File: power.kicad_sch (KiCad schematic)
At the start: 47 parts, among them CN3 DF40C-20DP-0.4V, J2 TYPE-C16PIN, Q5 CSD17575Q3A, Q6 CSD17575Q3A, Q7 CSD17575Q3A, Q8 CSD17575Q3A, U2 CH224K, U3 BQ25792RQMR, U4 AP2112K-3.3TRG1, U5 AP2112K-1.8TRG1, U6 LP8556SQ-E09/NOPB, U8 ESD7104MUTAG_C2987068, U9 TPS61088RHLR

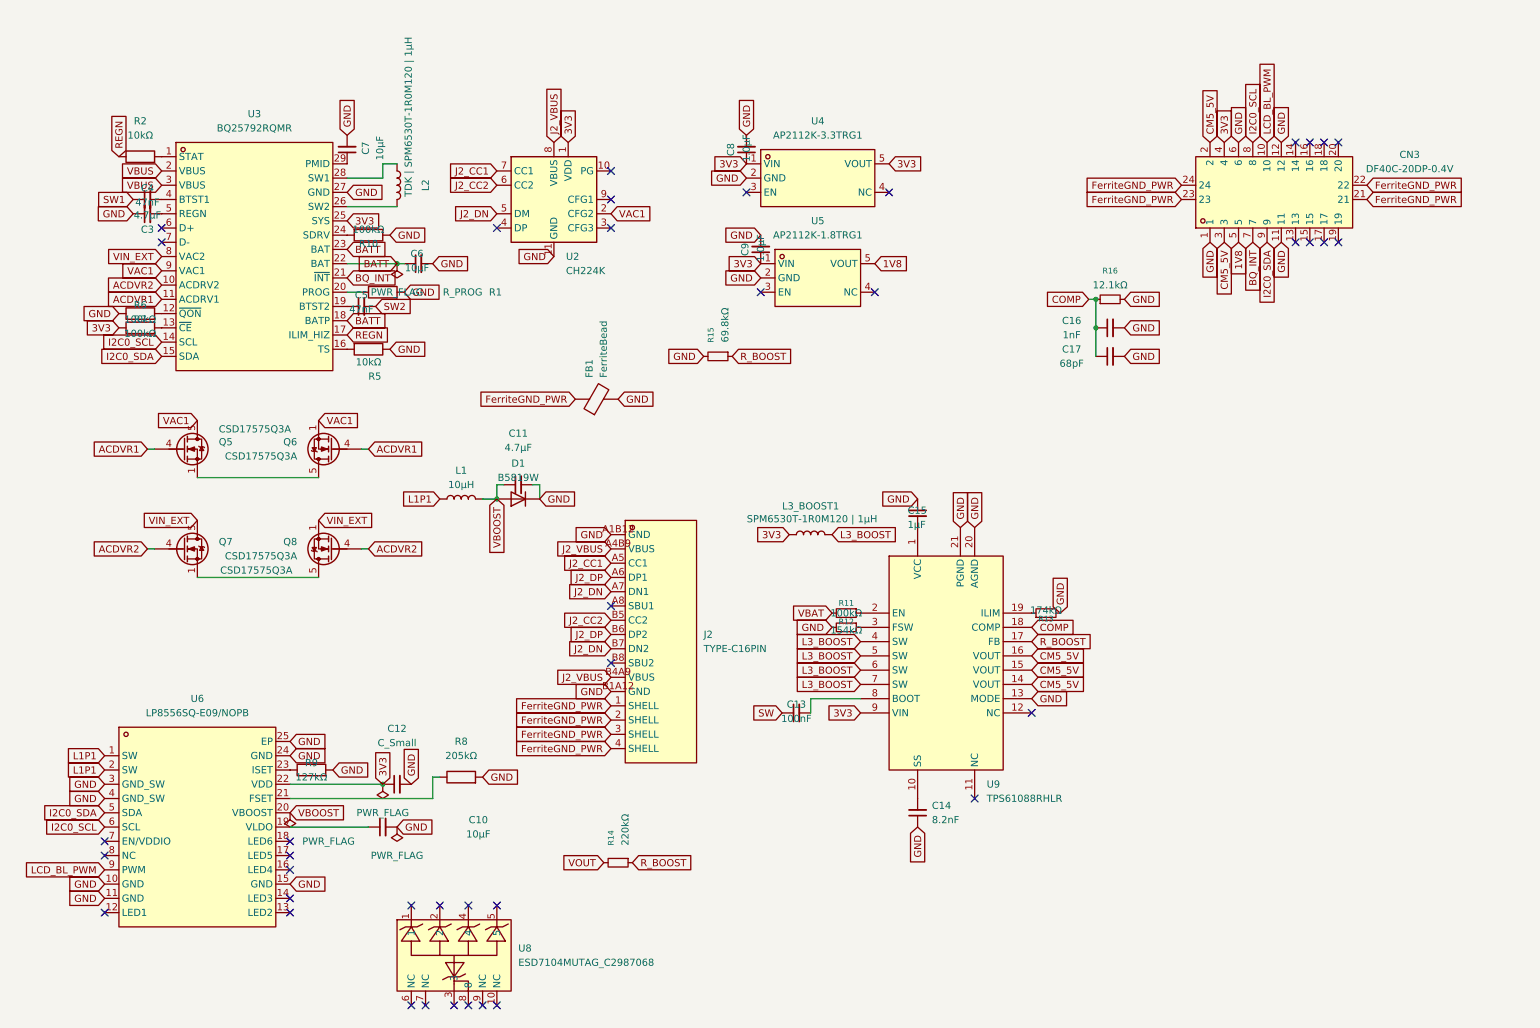
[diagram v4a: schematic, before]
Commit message: finished slateconnect i2c gpio expander, completed led status bar schematic, fixed all drc errors, started assigning footprints and started bom
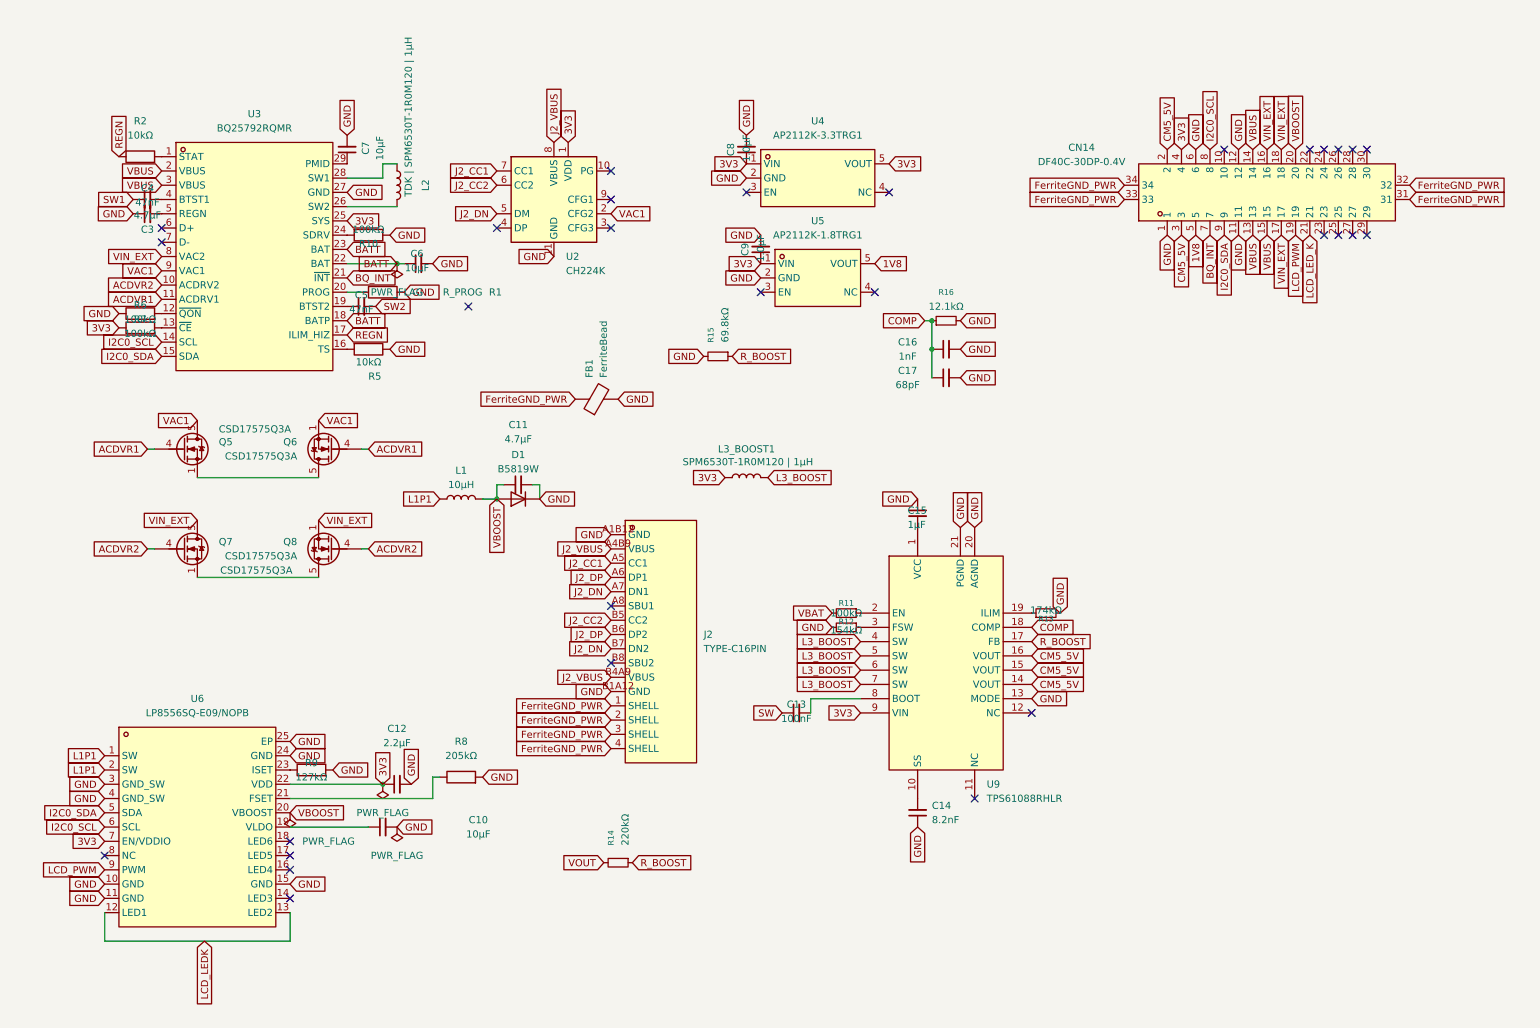
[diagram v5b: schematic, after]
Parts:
- removed CN3: DF40C-20DP-0.4V, slate113:CONN-SMD_20P-P0.40_HRS_DF40TC-20DP-0.4V, symbol slate113:DF40C-20DP-0.4V
- removed U8: ESD7104MUTAG_C2987068, slate113:DFN-10_L2.5-W1.0-P0.50-BL, symbol slate113:ESD7104MUTAG_C2987068
- added CN14: DF40C-30DP-0.4V, slate113:CONN-SMD_30P-P0.40_5001-BM0430-15-00, symbol slate113:DF40C-30DP-0.4V
- C10, C6, C7: footprint (none) -> Capacitor_SMD:C_0603_1608Metric; MPN (none) -> CL10A106KP8NNNC; Manufacturer (none) -> Samsung Electro-Mechanics
- C11, C3: footprint (none) -> Capacitor_SMD:C_0603_1608Metric; MPN (none) -> CL10B475KA8NNNC; Manufacturer (none) -> Samsung Electro-Mechanics
- C12: value C_Small -> 2.2µF; footprint (none) -> Capacitor_SMD:C_0603_1608Metric; MPN (none) -> CL10B225KA8NNNC; Manufacturer (none) -> Samsung Electro-Mechanics
- C13: footprint (none) -> Capacitor_SMD:C_0603_1608Metric; MPN (none) -> CL10B104KB8NNNC; Manufacturer (none) -> Samsung Electro-Mechanics
- C15, C8, C9: footprint (none) -> Capacitor_SMD:C_0603_1608Metric; MPN (none) -> CL10B105KA8NNNC; Manufacturer (none) -> Samsung Electro-Mechanics
- C16: footprint (none) -> Capacitor_SMD:C_0603_1608Metric; MPN (none) -> CL10B102KB8NNNC; Manufacturer (none) -> Samsung Electro-Mechanics
- C17: footprint (none) -> Capacitor_SMD:C_0603_1608Metric; MPN (none) -> CL10C680JB8NNNC; Manufacturer (none) -> Samsung Electro-Mechanics
- C4, C5: footprint (none) -> Capacitor_SMD:C_0603_1608Metric; MPN (none) -> CL10B473KB8NNNC; Manufacturer (none) -> Samsung Electro-Mechanics
- D1: MPN (none) -> B5819W; Manufacturer (none) -> LCSC
- L1: MPN (none) -> TDK SPM6530T-100M; Manufacturer (none) -> DigiKey
- Q5, Q6, Q7, Q8: MPN (none) -> CSD17575Q3A; Manufacturer (none) -> LCSC
- R10, R11, R6, R7: footprint (none) -> Resistor_SMD:R_0603_1608Metric; MPN (none) -> RC0603FR-07100KL; Manufacturer (none) -> Yageo
- R12: footprint (none) -> Resistor_SMD:R_0603_1608Metric; MPN (none) -> RC0603FR-07154KL; Manufacturer (none) -> Yageo
- R13: footprint (none) -> Resistor_SMD:R_0603_1608Metric; MPN (none) -> RC0603FR-07174KL; Manufacturer (none) -> Yageo
- R14: footprint (none) -> Resistor_SMD:R_0603_1608Metric; MPN (none) -> RC0603FR-07220KL; Manufacturer (none) -> Yageo
- R15: footprint (none) -> Resistor_SMD:R_0603_1608Metric; MPN (none) -> RC0603FR-0769K8L; Manufacturer (none) -> Yageo
- R16: footprint (none) -> Resistor_SMD:R_0603_1608Metric; MPN (none) -> RC0603FR-0712K1L; Manufacturer (none) -> Yageo
- R2, R5: footprint (none) -> Resistor_SMD:R_0603_1608Metric; MPN (none) -> RC0603FR-0710KL; Manufacturer (none) -> Yageo
- R8: footprint (none) -> Resistor_SMD:R_0603_1608Metric; MPN (none) -> RC0603FR-07205KL; Manufacturer (none) -> Yageo
- R9: footprint (none) -> Resistor_SMD:R_0603_1608Metric; MPN (none) -> RC0603FR-07127KL; Manufacturer (none) -> Yageo
- U2: MPN (none) -> CH224K; Manufacturer (none) -> LCSC
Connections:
- net 1V8: now also CN14.5
- net 3V3: now also U6.7 (EN/VDDIO), CN14.4
- net BQ_INT: now also CN14.7
- net CM5_5V: now also CN14.2, CN14.3
- net FerriteGND_PWR: now also CN14.31, CN14.32, CN14.33, CN14.34
- net GND: now also CN14.1, CN14.11, CN14.12, CN14.6
- net I2C0_SCL: now also CN14.8
- net I2C0_SDA: now also CN14.9
- net VBOOST: now also CN14.20
- net VBUS: now also CN14.13, CN14.14, CN14.15
- net VIN_EXT: now also CN14.16, CN14.17, CN14.18
- net LCD_LEDK: now reaches U6.12 (LED1)
- net LCD_LEDK: now also U6.13 (LED2)
- net LCD_BL_PWM renamed LCD_PWM
- net LCD_PWM: now also CN14.19
- new net LCD_LED_K: CN14.21
- no-connect marks 40 -> 30
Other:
- moved on the sheet: C16, C17, L3_BOOST1, R16

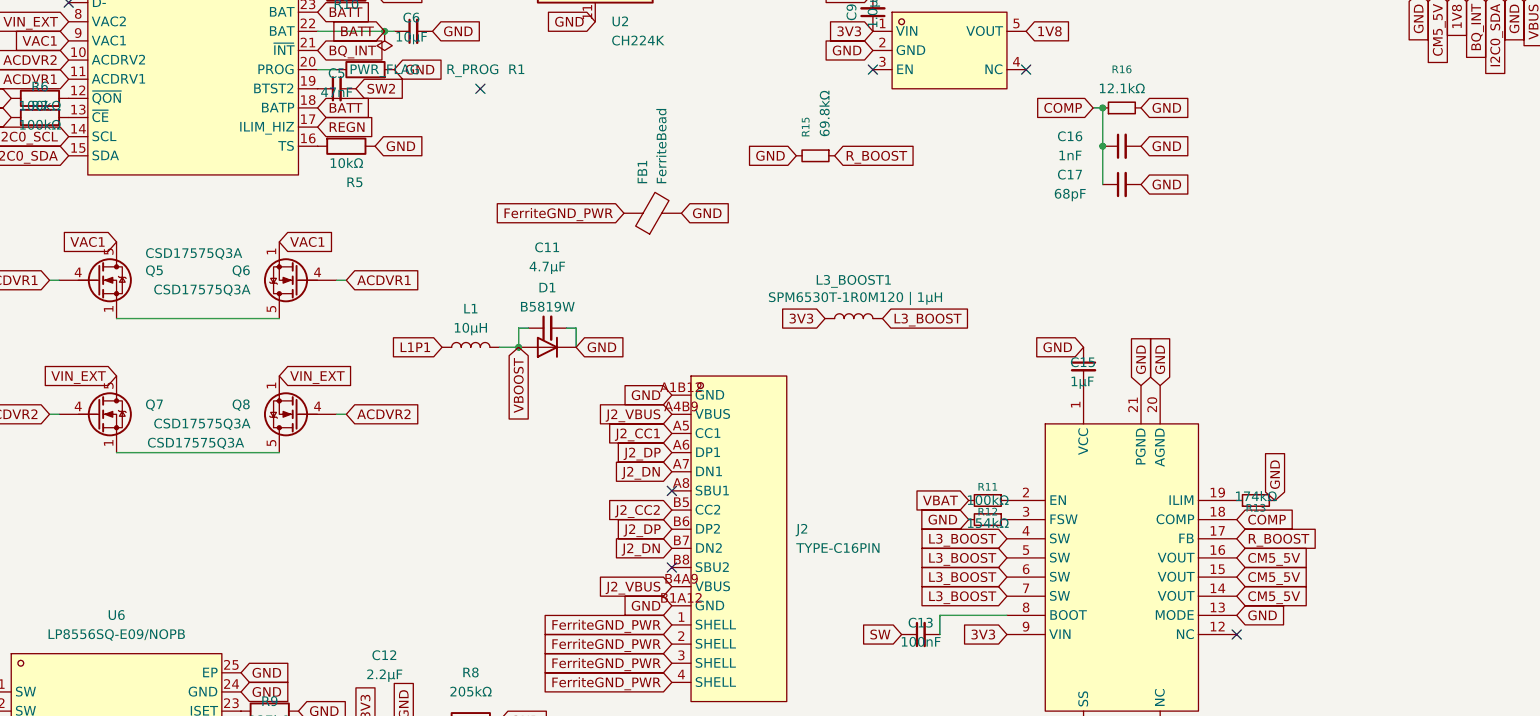
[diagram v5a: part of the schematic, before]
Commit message: assigned footprints and mpns across schematics + added 3d models and footprint libraries
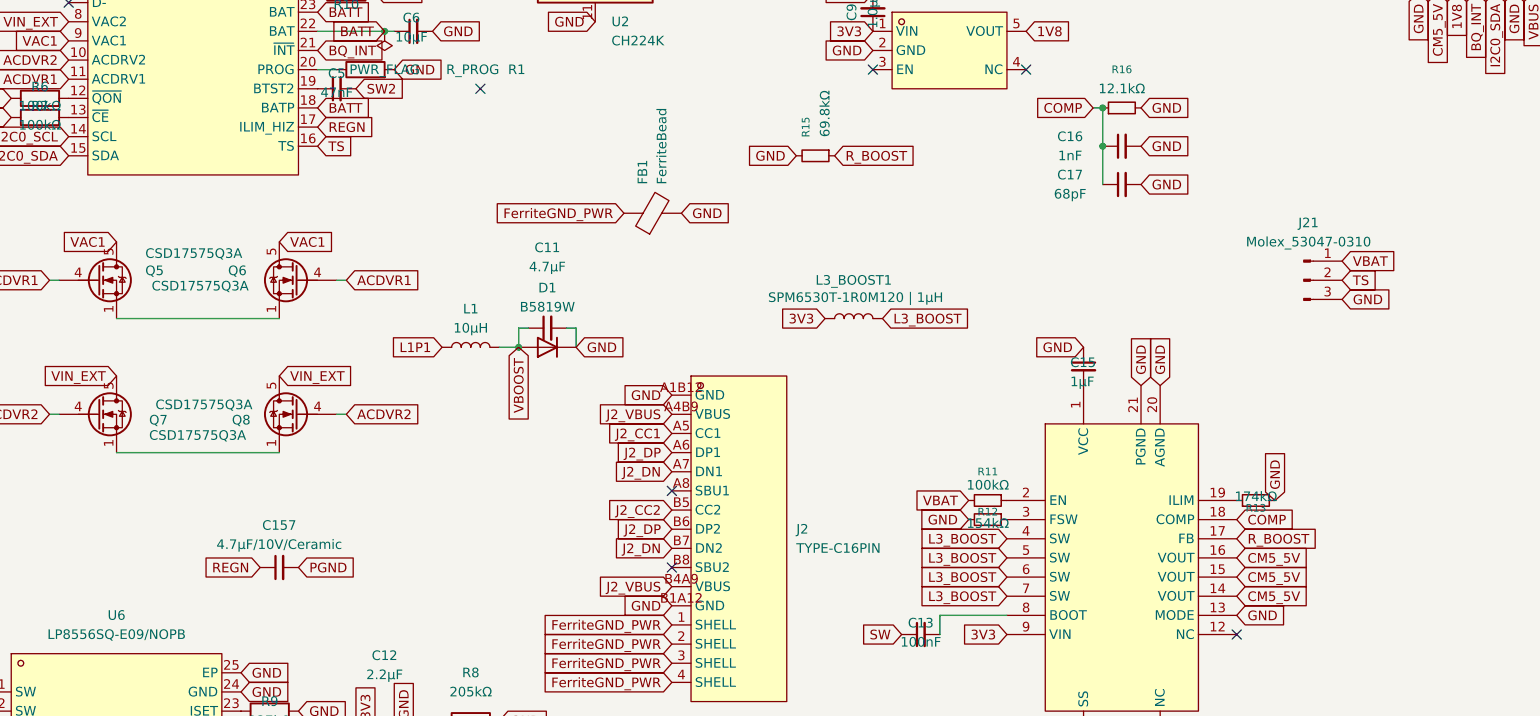
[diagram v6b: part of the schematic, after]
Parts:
- removed R5: 10kΩ, Resistor_SMD:R_0603_1608Metric, symbol Device:R
- added C157: 4.7µF/10V/Ceramic, Capacitor_SMD:C_0603_1608Metric, symbol Device:C_Small
- added J21: Molex_53047-0310, symbol Connector:Conn_01x03_Pin
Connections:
- net GND: now also J21.3 (Pin_3)
- net REGN: now also C157.1
- net VAC1: now also Q6.5 (D); no longer Q6.1 (S), Q6.2 (S), Q6.3 (S)
- net VBAT: now also J21.1 (Pin_1)
- net VIN_EXT: now also Q8.5 (D); no longer Q8.1 (S), Q8.2 (S), Q8.3 (S)
- net TS: now reaches U3.16 (TS)
- net TS: now also J21.2 (Pin_2)
- net at Q5.1 (S), Q5.2 (S), Q5.3 (S): now also Q6.1 (S), Q6.2 (S), Q6.3 (S); no longer Q6.5 (D)
- net at Q7.1 (S), Q7.2 (S), Q7.3 (S): now also Q8.1 (S), Q8.2 (S), Q8.3 (S); no longer Q8.5 (D)
- new net PGND: C157.2
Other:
- moved on the sheet: Q6, Q8

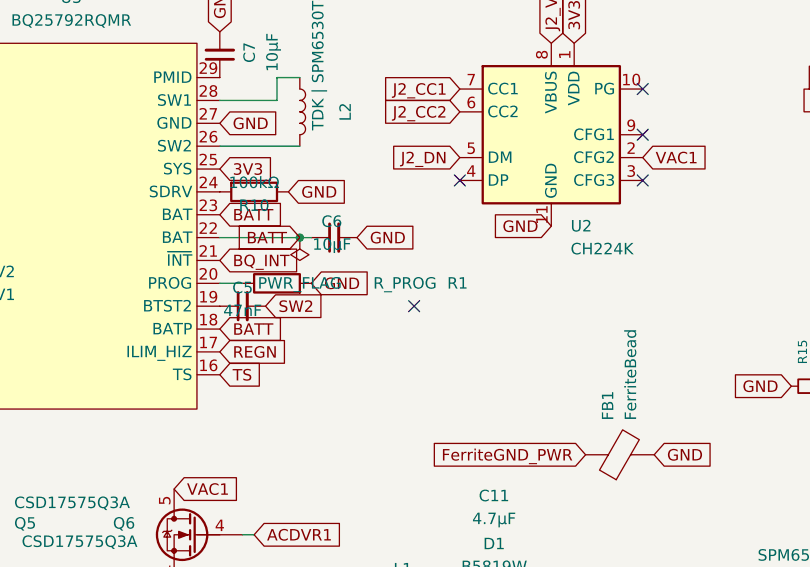
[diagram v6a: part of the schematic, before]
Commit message: finished BOM, replaced discontinued parts, added missing footprints, updated schematics and libraries
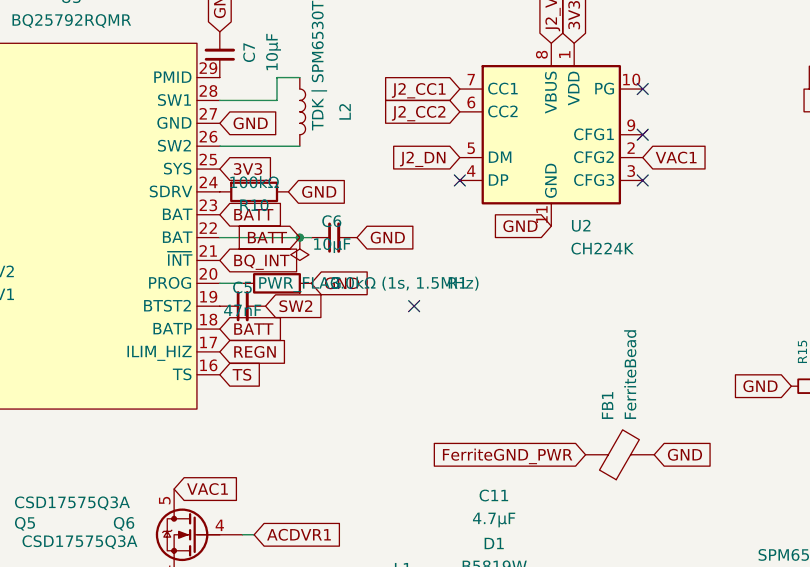
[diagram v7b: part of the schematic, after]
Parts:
- C10, C6, C7: LCSC Part (none) -> C380317; MPN CL10A106KP8NNNC -> TCC0603X5R106M160CT
- C11, C3: LCSC Part (none) -> C49326377; MPN CL10B475KA8NNNC -> 0603X5R475K160NT
- C12: LCSC Part (none) -> C49326370; MPN CL10B225KA8NNNC -> 0603X5R225K350NT
- C13: LCSC Part (none) -> C14663; MPN CL10B104KB8NNNC -> CC0603KRX7R9BB104
- C14: LCSC Part (none) -> C1322360; MPN (none) -> 0603B822K500NT
- C15, C8, C9: LCSC Part (none) -> C49326357; MPN CL10B105KA8NNNC -> 0603X5R105K160NT
- C157: LCSC Part (none) -> C49326377; MPN CL10B225KA8NNNC -> 0603X5R475K160NT
- C16: LCSC Part (none) -> C100040; MPN CL10B102KB8NNNC -> CC0603KRX7R9BB102
- C17: LCSC Part (none) -> C1680; MPN CL10C680JB8NNNC -> 0603CG680J500NT
- C4, C5: LCSC Part (none) -> C49326646; MPN CL10B473KB8NNNC -> 0603X7R473J500NT
- D1: DigiKey Part (none) -> 4786-B5819WTR-ND; LCSC Part (none) -> C64885
- FB1: footprint (none) -> Inductor_SMD:L_0603_1608Metric; LCSC Part (none) -> C107335; MPN (none) -> MPZ1608S601ATA00; Manufacturer (none) -> TDK
- J21: DigiKey Part (none) -> WM1732-ND; LCSC Part (none) -> C122442; MPN (none) -> 530470310
- L1: DigiKey Part (none) -> 445-SPM6530T-100MTR-ND; LCSC Part (none) -> C112288; MPN TDK SPM6530T-100M -> SPM6530T-100M
- L2, L3_BOOST1: DigiKey Part (none) -> 445-3880-2-ND; LCSC Part (none) -> C87572; MPN (none) -> SPM6530T-1R0M120
- Q5, Q6, Q7, Q8: LCSC Part (none) -> C529277; MPN CSD17575Q3A -> CSD17575Q3
- R1: value R_PROG -> 3.0kΩ (1s, 1.5MHz); footprint (none) -> Resistor_SMD:R_0603_1608Metric; LCSC Part (none) -> C4211; MPN (none) -> 0603WAF3001T5E
- R10, R11, R6, R7: LCSC Part (none) -> C25803; MPN RC0603FR-07100KL -> 0603WAF1003T5E
- R12: LCSC Part (none) -> C22881; MPN RC0603FR-07154KL -> 0603WAF1543T5E
- R13: LCSC Part (none) -> C2092939; MPN RC0603FR-07174KL -> 1-2176090-3
- R14: LCSC Part (none) -> C22961; MPN RC0603FR-07220KL -> 0603WAF2203T5E
- R15: LCSC Part (none) -> C23098; MPN RC0603FR-0769K8L -> 0603WAF6982T5E
- R16: LCSC Part (none) -> C22864; MPN RC0603FR-0712K1L -> 0603WAF1212T5E
- R2: LCSC Part (none) -> C25804; MPN RC0603FR-0710KL -> 0603WAF1002T5E
- R8: LCSC Part (none) -> C22949; MPN RC0603FR-07205KL -> 0603WAF2053T5E
- R9: LCSC Part (none) -> C22869; MPN RC0603FR-07127KL -> 0603WAF1273T5E
- U2: LCSC Part (none) -> C970725
